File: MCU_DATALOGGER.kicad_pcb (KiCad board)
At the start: 2 copper layers, 45.5 x 29.8 mm, 29 parts, among them J1 Conn_01x04_Pin, J2 Conn_01x09_Pin, J3 Conn_01x04_Pin, J4 Conn_02x03_Odd_Even, U1 24LC1025, U2 24LC1025, U3 DS1337S_, U4 ATMEGA328P-AU, Y1 32.768 KHz, Y2 16 MHz

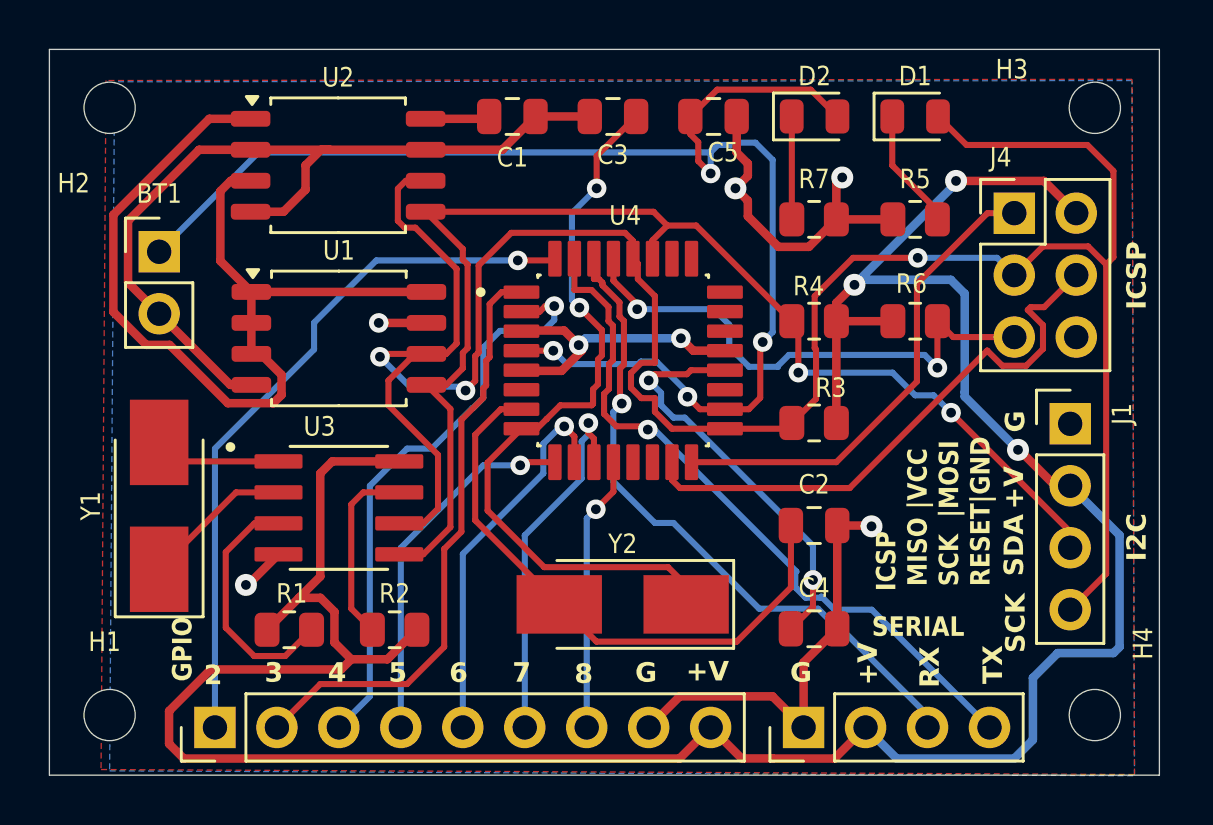
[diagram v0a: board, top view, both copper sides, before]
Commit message: Completed routing of 4 layer PCB
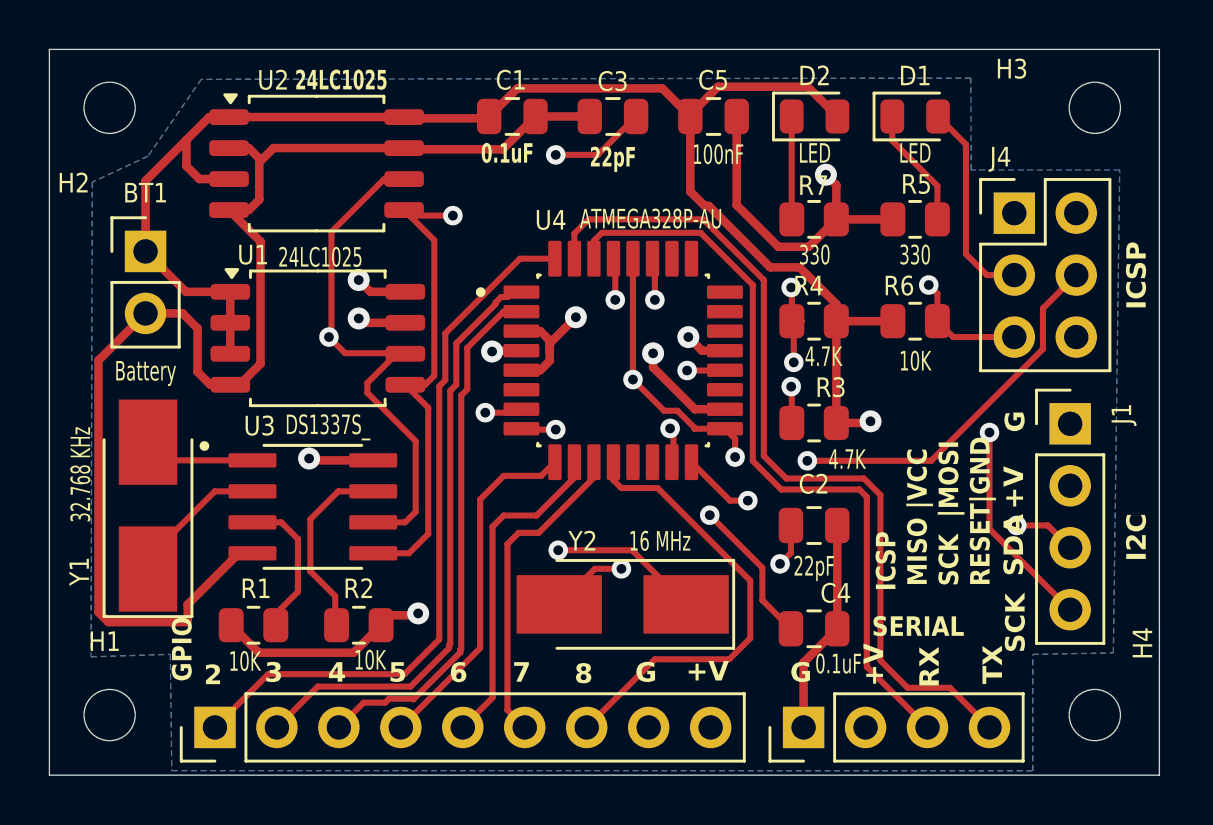
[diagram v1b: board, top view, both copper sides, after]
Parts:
- moved R1 1.48 mm to (130.9, 93.9)
- moved R2 1.48 mm to (135.2, 93.9)
- moved U3 1.07 mm to (133.3, 89.0)
- moved U2 0.89 mm to (133.5, 74.9)
- moved U1 0.86 mm to (133.5, 82.1)
- moved BT1 0.56 mm to (126.4, 78.5)
- moved Y1 0.46 mm to (126.5, 89.0)
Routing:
- net /VCC: track 215.1 -> 89.4 mm, vias 7 -> 6
- net /SCK: track 99.6 -> 85.4 mm, vias 3 -> 5
- net GND: track 81.9 -> 90.2 mm, vias 7 -> 4
- net /D8: track 11.3 -> 18.6 mm, vias 1 -> 0
- net /TX: track 29.2 -> 35.1 mm, vias 1 -> 0
- net Net-(U3-~{INTA}): track 10.2 -> 6.06 mm
- net /RX: track 27.4 -> 31.2 mm, vias 1 -> 0
- net Net-(U4-PB7): track 31.2 -> 27.8 mm, vias 2 -> 3
- net /SDA: track 53.0 -> 56.0 mm, vias 2 -> 5
- net /MISO: track 19.8 -> 22.2 mm, vias 0 -> 1
- net /D4: track 24.0 -> 21.7 mm, vias 1 -> 0
- net /D6: track 15.9 -> 13.6 mm, vias 1 -> 0
- net /D7: track 15.3 -> 13.1 mm, vias 1 -> 0
- net /RESET: track 22.1 -> 20.4 mm
- net Net-(U4-AREF): track 16.9 -> 15.6 mm
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- added copper zone on In2.Cu, net /VCC
- removed copper zone on F.Cu, net /VCC
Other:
- copper layers 2 -> 4
- board text added: "A 4 Layer MCU Datalogger PCB"
- board text removed: "A 2 Layer MCU Datalogger PCB"

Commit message: Added board characteristics of 4 layer PCB
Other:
- board text added: "0.0000 mm / 0.0000 mm"
- board text added: "0.3000 mm"
- board text added: "1.6000 mm"
- board text added: "45.5000 mm x 29.7500 mm"
- board text added: "BOARD CHARACTERISTICS"
- board text added: "Board Thickness:"
- board text added: "Board overall dimensions:"
- board text added: "Castellated pads:"
- board text added: "Copper Finish:"
- board text added: "Copper Layer Count:"
- board text added: "Edge card connectors:"
- board text added: "Impedance Control:"
- board text added: "Min hole diameter:"
- board text added: "Min track/spacing:"
- board text added: "No"
- board text added: "None"
- board text added: "Plated Board Edge:"
